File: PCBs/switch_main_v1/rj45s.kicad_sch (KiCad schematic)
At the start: 1 part, among them J901 TMJG46945AENL

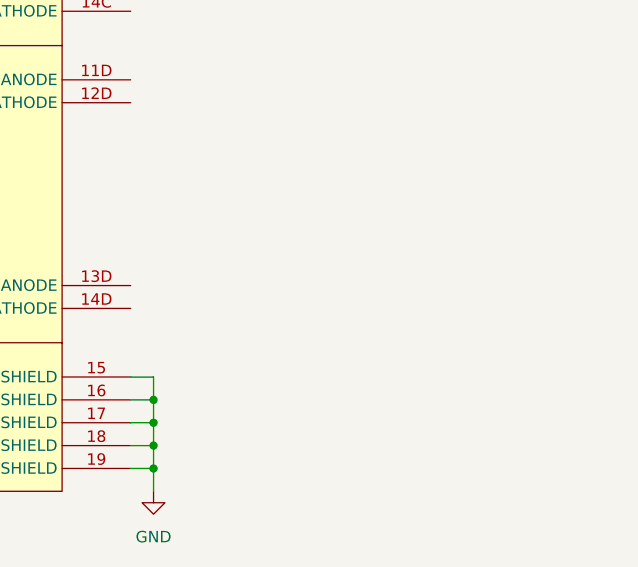
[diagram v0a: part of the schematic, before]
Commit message: Connectors schematic almost complete
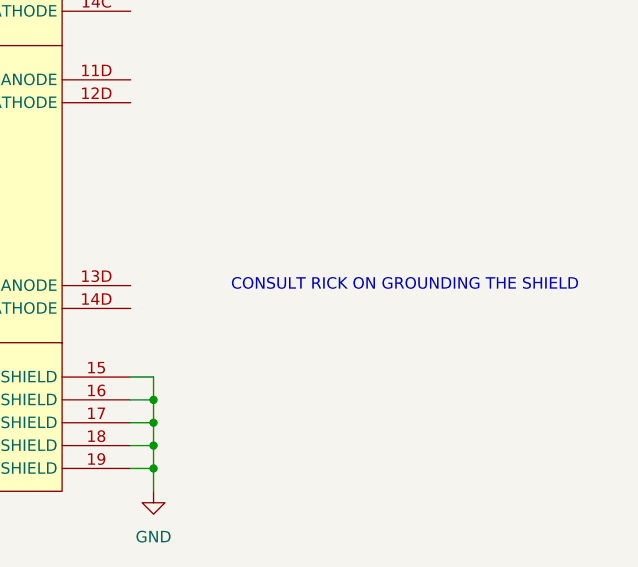
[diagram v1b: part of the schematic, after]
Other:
- note added: "CONSULT RICK ON GROUNDING THE SHIELD"
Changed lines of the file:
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@@
+		)
+	)
+	(text "CONSULT RICK ON GROUNDING THE SHIELD"
+		(exclude_from_sim no)
+		(at 185.42 152.4 0)
+		(effects
+			(font
+				(size 1.27 1.27)
+			)
 		)
 	)

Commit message: Schematic progress
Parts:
- added C901: C_Small, Capacitor_SMD:C_0402_1005Metric, symbol Device:C_Small
- added R901: R_Small, Resistor_SMD:R_0402_1005Metric, symbol Device:R_Small
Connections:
- net GND: now also C901.1, R901.1; no longer J901.15 (SHIELD), J901.16 (SHIELD), J901.17 (SHIELD), J901.18 (SHIELD), J901.19 (SHIELD)
- net ETHERNET_1.TD0_P: now reaches J901.2A (TD1+)
- net ETHERNET_2.TD0_P: now reaches J901.2B (TD1+)
- net ETHERNET_3.TD0_P: now reaches J901.2C (TD1+)
- net ETHERNET_4.TD0_P: now reaches J901.2D (TD1+)
- net ETHERNET_1.TD0_N: now reaches J901.3A (TD1-)
- net ETHERNET_2.TD0_N: now reaches J901.3B (TD1-)
- net ETHERNET_3.TD0_N: now reaches J901.3C (TD1-)
- net ETHERNET_4.TD0_N: now reaches J901.3D (TD1-)
- net ETHERNET_1.TD1_P: now reaches J901.4A (TD2+)
- net ETHERNET_2.TD1_P: now reaches J901.4B (TD2+)
- net ETHERNET_3.TD1_P: now reaches J901.4C (TD2+)
- net ETHERNET_4.TD1_P: now reaches J901.4D (TD2+)
- net ETHERNET_1.TD1_N: now reaches J901.5A (TD2-)
- net ETHERNET_2.TD1_N: now reaches J901.5B (TD2-)
- net ETHERNET_3.TD1_N: now reaches J901.5C (TD2-)
- net ETHERNET_4.TD1_N: now reaches J901.5D (TD2-)
- net ETHERNET_1.TD2_P: now reaches J901.6A (TD3+)
- net ETHERNET_2.TD2_P: now reaches J901.6B (TD3+)
- net ETHERNET_3.TD2_P: now reaches J901.6C (TD3+)
- net ETHERNET_4.TD2_P: now reaches J901.6D (TD3+)
- net ETHERNET_1.TD2_N: now reaches J901.7A (TD3-)
- net ETHERNET_2.TD2_N: now reaches J901.7B (TD3-)
- net ETHERNET_3.TD2_N: now reaches J901.7C (TD3-)
- net ETHERNET_4.TD2_N: now reaches J901.7D (TD3-)
- net ETHERNET_1.TD3_P: now reaches J901.8A (TD4+)
- net ETHERNET_2.TD3_P: now reaches J901.8B (TD4+)
- net ETHERNET_3.TD3_P: now reaches J901.8C (TD4+)
- net ETHERNET_4.TD3_P: now reaches J901.8D (TD4+)
- net ETHERNET_1.TD3_N: now reaches J901.9A (TD4-)
- net ETHERNET_2.TD3_N: now reaches J901.9B (TD4-)
- net ETHERNET_3.TD3_N: now reaches J901.9C (TD4-)
- net ETHERNET_4.TD3_N: now reaches J901.9D (TD4-)
- new net Earth: C901.2, J901.15 (SHIELD), J901.16 (SHIELD), J901.17 (SHIELD), J901.18 (SHIELD), J901.19 (SHIELD), R901.2

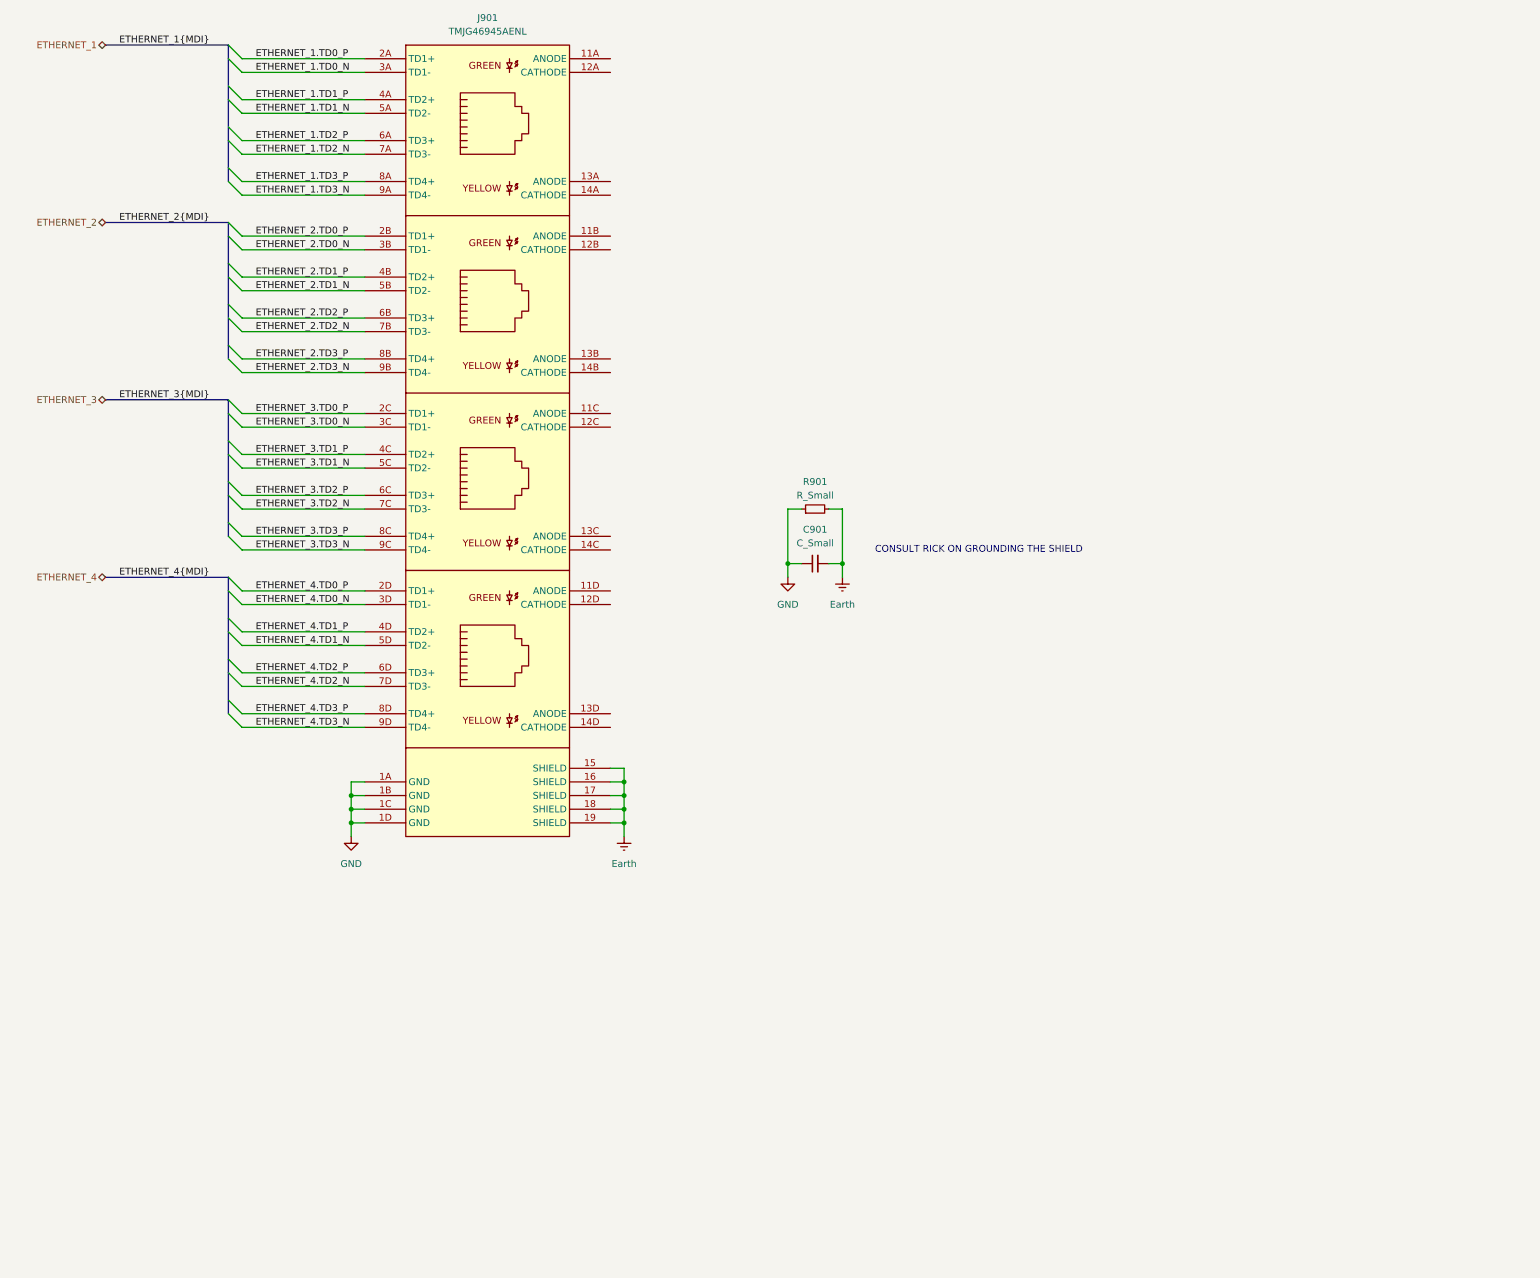
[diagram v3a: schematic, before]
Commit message: GbE part of schematic done
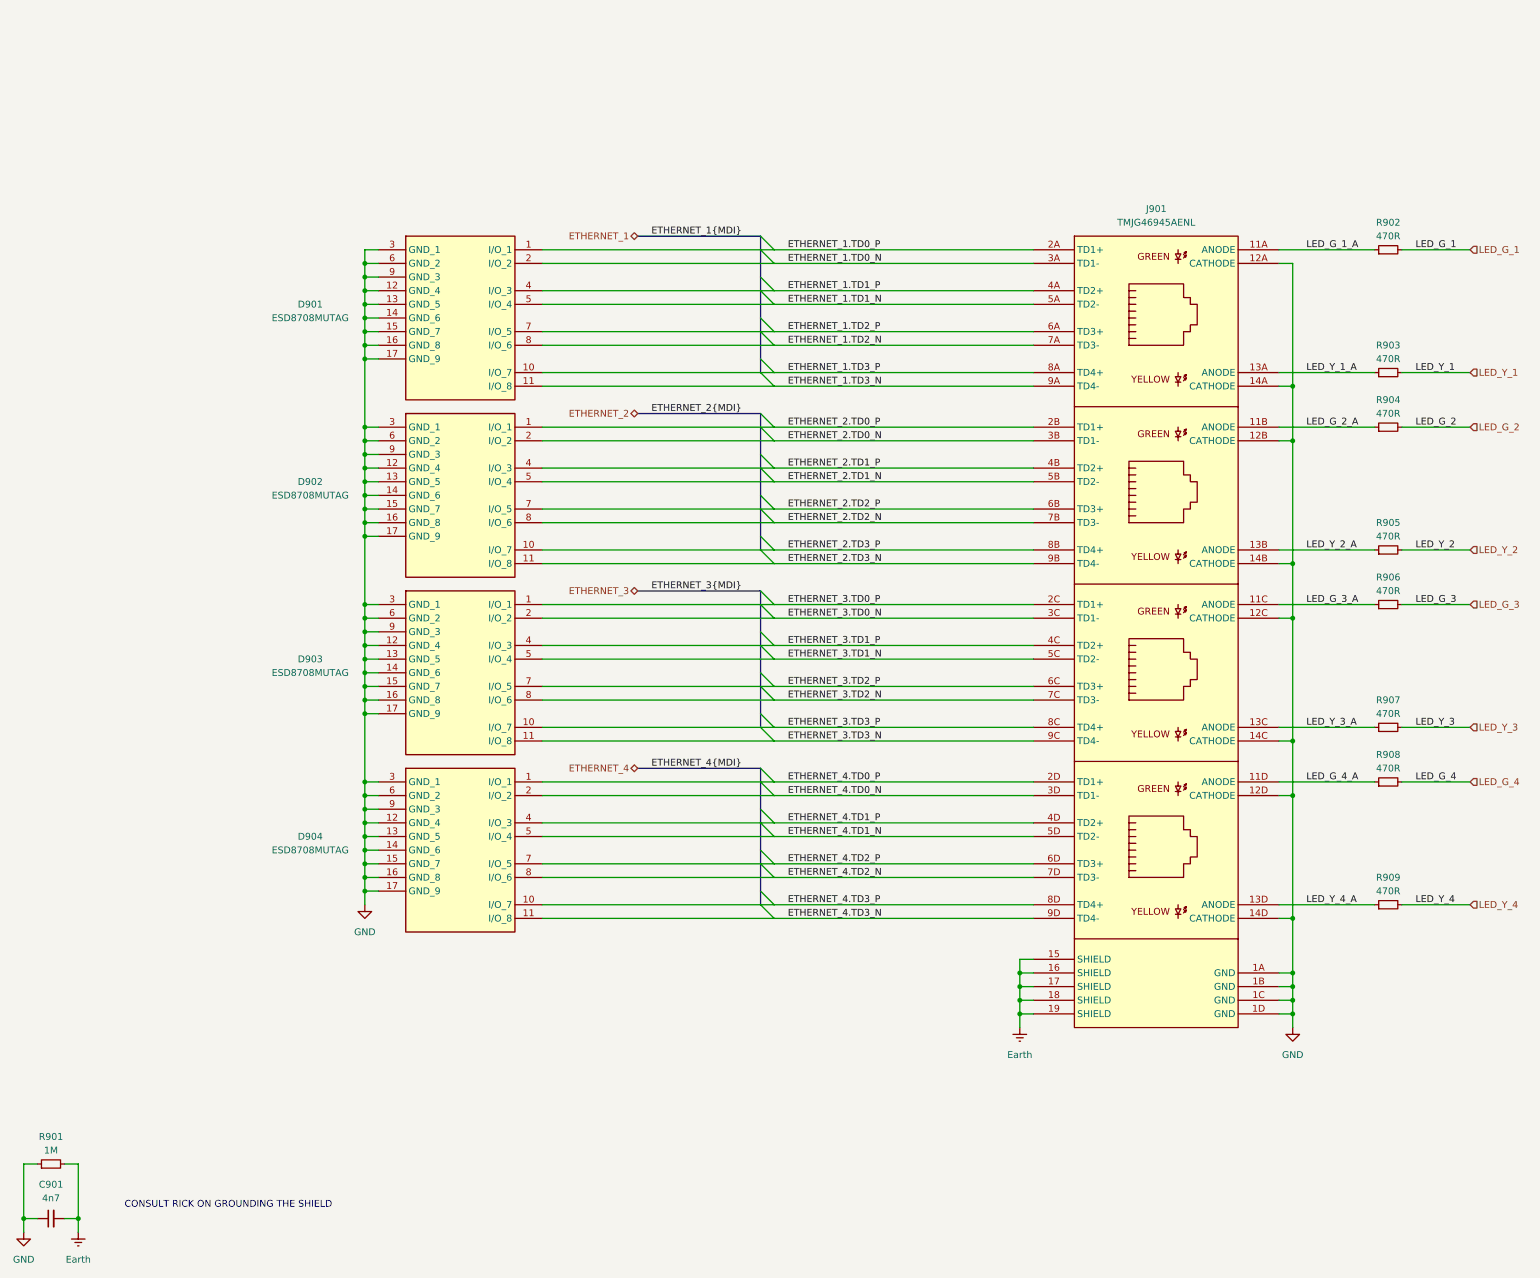
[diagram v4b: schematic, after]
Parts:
- added D901, D902, D903, D904: ESD8708MUTAG, switch_footprints:ESD8708MUTAG, symbol ESD8708MUTAG:ESD8708MUTAG
- added R902, R903, R904, R905, R906, R907, R908, R909: 470R, Resistor_SMD:R_0402_1005Metric, symbol Device:R_Small
- C901: value C_Small -> 4n7
- R901: value R_Small -> 1M
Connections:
- net ETHERNET_1.TD0_N: now also D901.2 (I/O_2)
- net ETHERNET_1.TD0_P: now also D901.1 (I/O_1)
- net ETHERNET_1.TD1_N: now also D901.5 (I/O_4)
- net ETHERNET_1.TD1_P: now also D901.4 (I/O_3)
- net ETHERNET_1.TD2_N: now also D901.8 (I/O_6)
- net ETHERNET_1.TD2_P: now also D901.7 (I/O_5)
- net ETHERNET_1.TD3_N: now also D901.11 (I/O_8)
- net ETHERNET_1.TD3_P: now also D901.10 (I/O_7)
- net ETHERNET_2.TD0_N: now also D902.2 (I/O_2)
- net ETHERNET_2.TD0_P: now also D902.1 (I/O_1)
- net ETHERNET_2.TD1_N: now also D902.5 (I/O_4)
- net ETHERNET_2.TD1_P: now also D902.4 (I/O_3)
- net ETHERNET_2.TD2_N: now also D902.8 (I/O_6)
- net ETHERNET_2.TD2_P: now also D902.7 (I/O_5)
- net ETHERNET_2.TD3_N: now also D902.11 (I/O_8)
- net ETHERNET_2.TD3_P: now also D902.10 (I/O_7)
- net ETHERNET_3.TD0_N: now also D903.2 (I/O_2)
- net ETHERNET_3.TD0_P: now also D903.1 (I/O_1)
- net ETHERNET_3.TD1_N: now also D903.5 (I/O_4)
- net ETHERNET_3.TD1_P: now also D903.4 (I/O_3)
- net ETHERNET_3.TD2_N: now also D903.8 (I/O_6)
- net ETHERNET_3.TD2_P: now also D903.7 (I/O_5)
- net ETHERNET_3.TD3_N: now also D903.11 (I/O_8)
- net ETHERNET_3.TD3_P: now also D903.10 (I/O_7)
- net ETHERNET_4.TD0_N: now also D904.2 (I/O_2)
- net ETHERNET_4.TD0_P: now also D904.1 (I/O_1)
- net ETHERNET_4.TD1_N: now also D904.5 (I/O_4)
- net ETHERNET_4.TD1_P: now also D904.4 (I/O_3)
- net ETHERNET_4.TD2_N: now also D904.8 (I/O_6)
- net ETHERNET_4.TD2_P: now also D904.7 (I/O_5)
- net ETHERNET_4.TD3_N: now also D904.11 (I/O_8)
- net ETHERNET_4.TD3_P: now also D904.10 (I/O_7)
- net GND: now also J901.12A (CATHODE), J901.12B (CATHODE), J901.12C (CATHODE), J901.12D (CATHODE), J901.14A (CATHODE), J901.14B (CATHODE), J901.14C (CATHODE), J901.14D (CATHODE), D901.12 (GND_4), D901.13 (GND_5), D901.14 (GND_6), D901.15 (GND_7), D901.16 (GND_8), D901.17 (GND_9), D901.3 (GND_1), D901.6 (GND_2), D901.9 (GND_3), D902.12 (GND_4), D902.13 (GND_5), D902.14 (GND_6), D902.15 (GND_7), D902.16 (GND_8), D902.17 (GND_9), D902.3 (GND_1), D902.6 (GND_2), D902.9 (GND_3), D903.12 (GND_4), D903.13 (GND_5), D903.14 (GND_6), D903.15 (GND_7), D903.16 (GND_8), D903.17 (GND_9), D903.3 (GND_1), D903.6 (GND_2), D903.9 (GND_3), D904.12 (GND_4), D904.13 (GND_5), D904.14 (GND_6), D904.15 (GND_7), D904.16 (GND_8), D904.17 (GND_9), D904.3 (GND_1), D904.6 (GND_2), D904.9 (GND_3)
- net LED_G_1_A: now reaches J901.11A (ANODE)
- net LED_G_1_A: now also R902.1
- net LED_G_2_A: now reaches J901.11B (ANODE)
- net LED_G_2_A: now also R904.1
- net LED_G_3_A: now reaches J901.11C (ANODE)
- net LED_G_3_A: now also R906.1
- net LED_G_4_A: now reaches J901.11D (ANODE)
- net LED_G_4_A: now also R908.1
- net LED_Y_1_A: now reaches J901.13A (ANODE)
- net LED_Y_1_A: now also R903.1
- net LED_Y_2_A: now reaches J901.13B (ANODE)
- net LED_Y_2_A: now also R905.1
- net LED_Y_3_A: now reaches J901.13C (ANODE)
- net LED_Y_3_A: now also R907.1
- net LED_Y_4_A: now reaches J901.13D (ANODE)
- net LED_Y_4_A: now also R909.1
- new net LED_G_1: R902.2
- new net LED_G_2: R904.2
- new net LED_G_3: R906.2
- new net LED_G_4: R908.2
- new net LED_Y_1: R903.2
- new net LED_Y_2: R905.2
- new net LED_Y_3: R907.2
- new net LED_Y_4: R909.2
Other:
- company: (none) -> Ben Smith
- title: (none) -> RJ45 Connectors
- moved on the sheet: C901, J901, R901
